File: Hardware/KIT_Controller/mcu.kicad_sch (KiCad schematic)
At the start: 27 parts, among them J201 USB_BOOT, J202 USB_B, U201 RP2040, U202 W25Q128JVS, U203 NCP1117-3.3_SOT223, Y201 Crystal

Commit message: add other junk idk
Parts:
- added U201: TCA9554DB, Package_SO:SSOP-16_5.3x6.2mm_P0.65mm, symbol Interface_Expansion:TCA9554DB
- added U204: HDSP-7401, Display_7Segment:HDSP-7401, symbol Display_Character:HDSP-7401
- renumbered C215 to C203, C214 to C204, C216 to C205, C203 to C206, C204 to C207, C205 to C208, C206 to C209, C207 to C210, C208 to C211, C209 to C212, C210 to C213, C211 to C214, C212 to C215, C213 to C216, J202 to J201, J201 to J202, R204 to R201, R205 to R202, R201 to R203, R202 to R204, R203 to R205, U201 to U205
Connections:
- no-connect marks 33 -> 59

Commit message: Add more stuff
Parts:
- added R206: 10k, Resistor_SMD:R_0805_2012Metric, symbol Device:R_Small
- added R207, R208, R209, R210, R211, R212, R213, R214: 240, Resistor_SMD:R_0805_2012Metric, symbol Device:R_Small
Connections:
- net +3V3: now also U201.16 (VDD), R206.2
- net GND: now also U201.1 (A0), U201.2 (A1), U201.3 (A2), U201.8 (GND), U204.1 (CA), U204.6 (CA)
- net at U201.10 (P5): now also R213.1
- net at U201.11 (P6): now also R210.1
- net at U201.12 (P7): now also R214.1
- net at U201.13 (~{INT}): now also R206.1
- net SCL: now reaches U201.14 (SCL)
- net SCL: now also U205.7 (GPIO5)
- net SDA: now reaches U201.15 (SDA)
- net SDA: now also U205.6 (GPIO4)
- net at U201.4 (P0): now also R207.1
- net at U201.5 (P1): now also R211.1
- net at U201.6 (P2): now also R208.1
- net at U201.7 (P3): now also R212.1
- net at U201.9 (P4): now also R209.1
- net MISO: now reaches U205.27 (GPIO16)
- net SCK: now reaches U205.29 (GPIO18)
- net MOSI: now reaches U205.30 (GPIO19)
- net at U204.10 (A): now also R207.2
- net at U204.2 (F): now also R213.2
- net at U204.3 (G): now also R210.2
- net at U204.4 (E): now also R209.2
- net at U204.5 (D): now also R212.2
- net at U204.7 (DP): now also R214.2
- net at U204.8 (C): now also R208.2
- net at U204.9 (B): now also R211.2
- no-connect marks 59 -> 28
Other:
- note added: "Clock"
- note added: "EEPROM"
- note added: "LLL corrosponds to Address 20 (32 in decimal)"
- note added: "USB"
- note added: "i2c status"
- company: (none) -> Kitsune Scientific
- title: (none) -> KIT Mainboard
- moved on the sheet: C206, C207, C208, C209, C210, C211, C212, C213, C214, C215, C216, R204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

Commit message: Fixup drc
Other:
- moved on the sheet: R207, R208, R209, R210
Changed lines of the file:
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@@
   (junction (at 172.085 36.83) (diameter 0) (color 0 0 0 0)
+  )
+  (junction (at 73.025 163.195) (diameter 0) (color 0 0 0 0)
   )
   (junction (at 24.13 178.435) (diameter 0) (color 0 0 0 0)
@@
     (stroke (width 0) (type default) (color 0 0 0 0))
   )
-  (wire (pts (xy 47.625 173.355) (xy 50.165 173.355))
+  (wire (pts (xy 47.625 173.355) (xy 52.07 173.355))
     (stroke (width 0) (type default) (color 0 0 0 0))
   )
@@
     (stroke (width 0) (type default) (color 0 0 0 0))
   )
-  (wire (pts (xy 55.245 163.195) (xy 73.025 163.195))
+  (wire (pts (xy 57.15 163.195) (xy 73.025 163.195))
     (stroke (width 0) (type default) (color 0 0 0 0))
   )
@@
     (stroke (width 0) (type default) (color 0 0 0 0))
   )
+  (wire (pts (xy 74.295 163.195) (xy 73.025 163.195))
+    (stroke (width 0) (type default) (color 0 0 0 0))
+  )
   (wire (pts (xy 36.83 78.74) (xy 46.99 78.74))
     (stroke (width 0) (type default) (color 0 0 0 0))
@@
     (stroke (width 0) (type default) (color 0 0 0 0))
   )
-  (wire (pts (xy 55.245 178.435) (xy 73.025 178.435))
+  (wire (pts (xy 57.15 178.435) (xy 73.025 178.435))
     (stroke (width 0) (type default) (color 0 0 0 0))
   )
@@
     (stroke (width 0) (type default) (color 0 0 0 0))
   )
-  (wire (pts (xy 47.625 178.435) (xy 50.165 178.435))
+  (wire (pts (xy 47.625 178.435) (xy 52.07 178.435))
     (stroke (width 0) (type default) (color 0 0 0 0))
   )
@@
     (stroke (width 0) (type default) (color 0 0 0 0))
   )
-  (wire (pts (xy 55.245 173.355) (xy 73.025 173.355))
+  (wire (pts (xy 57.15 173.355) (xy 73.025 173.355))
     (stroke (width 0) (type default) (color 0 0 0 0))
   )
@@
     (stroke (width 0) (type default) (color 0 0 0 0))
   )
-  (wire (pts (xy 55.245 168.275) (xy 73.025 168.275))
+  (wire (pts (xy 57.15 168.275) (xy 73.025 168.275))
     (stroke (width 0) (type default) (color 0 0 0 0))
   )
@@
     (stroke (width 0) (type default) (color 0 0 0 0))
   )
-  (wire (pts (xy 47.625 163.195) (xy 50.165 163.195))
+  (wire (pts (xy 47.625 163.195) (xy 52.07 163.195))
     (stroke (width 0) (type default) (color 0 0 0 0))
   )
@@
     (stroke (width 0) (type default) (color 0 0 0 0))
   )
-  (wire (pts (xy 47.625 168.275) (xy 50.165 168.275))
+  (wire (pts (xy 47.625 168.275) (xy 52.07 168.275))
     (stroke (width 0) (type default) (color 0 0 0 0))
   )
@@
     (pin "2")
   )
-  (symbol (lib_id "Device:R_Small") (at 52.705 173.355 90) (unit 1)
-    (in_bom yes) (on_board yes)
-    (property "Reference" "R209" (id 0) (at 49.53 172.085 90))
-    (property "Value" "240" (id 1) (at 52.705 173.355 90))
-    (property "Footprint" "Resistor_SMD:R_0805_2012Metric" (id 2) (at 52.705 173.355 0)
-      (effects (font (size 1.27 1.27)) hide)
-    )
-    (property "Datasheet" "~" (id 3) (at 52.705 173.355 0)
+  (symbol (lib_id "Device:R_Small") (at 54.61 173.355 90) (unit 1)
+    (in_bom yes) (on_board yes)
+    (property "Reference" "R209" (id 0) (at 50.165 172.085 90))
+    (property "Value" "240" (id 1) (at 54.61 173.355 90))
+    (property "Footprint" "Resistor_SMD:R_0805_2012Metric" (id 2) (at 54.61 173.355 0)
+      (effects (font (size 1.27 1.27)) hide)
+    )
+    (property "Datasheet" "~" (id 3) (at 54.61 173.355 0)
       (effects (font (size 1.27 1.27)) hide)
     )
@@
   (symbol (lib_id "Device:R_Small") (at 64.135 175.895 90) (unit 1)
     (in_bom yes) (on_board yes)
-    (property "Reference" "R213" (id 0) (at 60.96 174.625 90))
+    (property "Reference" "R213" (id 0) (at 59.69 174.625 90))
     (property "Value" "240" (id 1) (at 64.135 175.895 90))
     (property "Footprint" "Resistor_SMD:R_0805_2012Metric" (id 2) (at 64.135 175.895 0)
@@
     (pin "2")
   )
-  (symbol (lib_id "Device:R_Small") (at 52.705 163.195 90) (unit 1)
-    (in_bom yes) (on_board yes)
-    (property "Reference" "R207" (id 0) (at 49.53 161.925 90))
-    (property "Value" "240" (id 1) (at 52.705 163.195 90))
-    (property "Footprint" "Resistor_SMD:R_0805_2012Metric" (id 2) (at 52.705 163.195 0)
-      (effects (font (size 1.27 1.27)) hide)
-    )
-    (property "Datasheet" "~" (id 3) (at 52.705 163.195 0)
+  (symbol (lib_id "Device:R_Small") (at 54.61 163.195 90) (unit 1)
+    (in_bom yes) (on_board yes)
+    (property "Reference" "R207" (id 0) (at 50.165 161.925 90))
+    (property "Value" "240" (id 1) (at 54.61 163.195 90))
+    (property "Footprint" "Resistor_SMD:R_0805_2012Metric" (id 2) (at 54.61 163.195 0)
+      (effects (font (size 1.27 1.27)) hide)
+    )
+    (property "Datasheet" "~" (id 3) (at 54.61 163.195 0)
       (effects (font (size 1.27 1.27)) hide)
     )
@@
   (symbol (lib_id "Device:R_Small") (at 64.135 165.735 90) (unit 1)
     (in_bom yes) (on_board yes)
-    (property "Reference" "R211" (id 0) (at 60.96 164.465 90))
+    (property "Reference" "R211" (id 0) (at 59.69 164.465 90))
     (property "Value" "240" (id 1) (at 64.135 165.735 90))
     (property "Footprint" "Resistor_SMD:R_0805_2012Metric" (id 2) (at 64.135 165.735 0)
@@
     (pin "3")
   )
-  (symbol (lib_id "Device:R_Small") (at 52.705 178.435 90) (unit 1)
-    (in_bom yes) (on_board yes)
-    (property "Reference" "R210" (id 0) (at 49.53 177.165 90))
-    (property "Value" "240" (id 1) (at 52.705 178.435 90))
-    (property "Footprint" "Resistor_SMD:R_0805_2012Metric" (id 2) (at 52.705 178.435 0)
-      (effects (font (size 1.27 1.27)) hide)
-    )
-    (property "Datasheet" "~" (id 3) (at 52.705 178.435 0)
+  (symbol (lib_id "Device:R_Small") (at 54.61 178.435 90) (unit 1)
+    (in_bom yes) (on_board yes)
+    (property "Reference" "R210" (id 0) (at 50.165 177.165 90))
+    (property "Value" "240" (id 1) (at 54.61 178.435 90))
+    (property "Footprint" "Resistor_SMD:R_0805_2012Metric" (id 2) (at 54.61 178.435 0)
+      (effects (font (size 1.27 1.27)) hide)
+    )
+    (property "Datasheet" "~" (id 3) (at 54.61 178.435 0)
       (effects (font (size 1.27 1.27)) hide)
     )
@@
   (symbol (lib_id "Device:R_Small") (at 64.135 170.815 90) (unit 1)
     (in_bom yes) (on_board yes)
-    (property "Reference" "R212" (id 0) (at 60.96 169.545 90))
+    (property "Reference" "R212" (id 0) (at 59.69 169.545 90))
     (property "Value" "240" (id 1) (at 64.135 170.815 90))
     (property "Footprint" "Resistor_SMD:R_0805_2012Metric" (id 2) (at 64.135 170.815 0)
@@
   (symbol (lib_id "Device:R_Small") (at 64.135 180.975 90) (unit 1)
     (in_bom yes) (on_board yes)
-    (property "Reference" "R214" (id 0) (at 60.96 179.705 90))
+    (property "Reference" "R214" (id 0) (at 59.69 179.705 90))
     (property "Value" "240" (id 1) (at 64.135 180.975 90))
     (property "Footprint" "Resistor_SMD:R_0805_2012Metric" (id 2) (at 64.135 180.975 0)
@@
     (pin "1")
   )
-  (symbol (lib_id "Device:R_Small") (at 52.705 168.275 90) (unit 1)
-    (in_bom yes) (on_board yes)
-    (property "Reference" "R208" (id 0) (at 49.53 167.005 90))
-    (property "Value" "240" (id 1) (at 52.705 168.275 90))
-    (property "Footprint" "Resistor_SMD:R_0805_2012Metric" (id 2) (at 52.705 168.275 0)
-      (effects (font (size 1.27 1.27)) hide)
-    )
-    (property "Datasheet" "~" (id 3) (at 52.705 168.275 0)
-      (effects (font (size 1.27 1.27)) hide)
-    )
+  (symbol (lib_id "Device:R_Small") (at 54.61 168.275 90) (unit 1)
+    (in_bom yes) (on_board yes)
+    (property "Reference" "R208" (id 0) (at 50.165 167.005 90))
+    (property "Value" "240" (id 1) (at 54.61 168.275 90))
+    (property "Footprint" "Resistor_SMD:R_0805_2012Metric" (id 2) (at 54.61 168.275 0)
+      (effects (font (size 1.27 1.27)) hide)
+    )
+    (property "Datasheet" "~" (id 3) (at 54.61 168.275 0)
+      (effects (font (size 1.27 1.27)) hide)
+    )

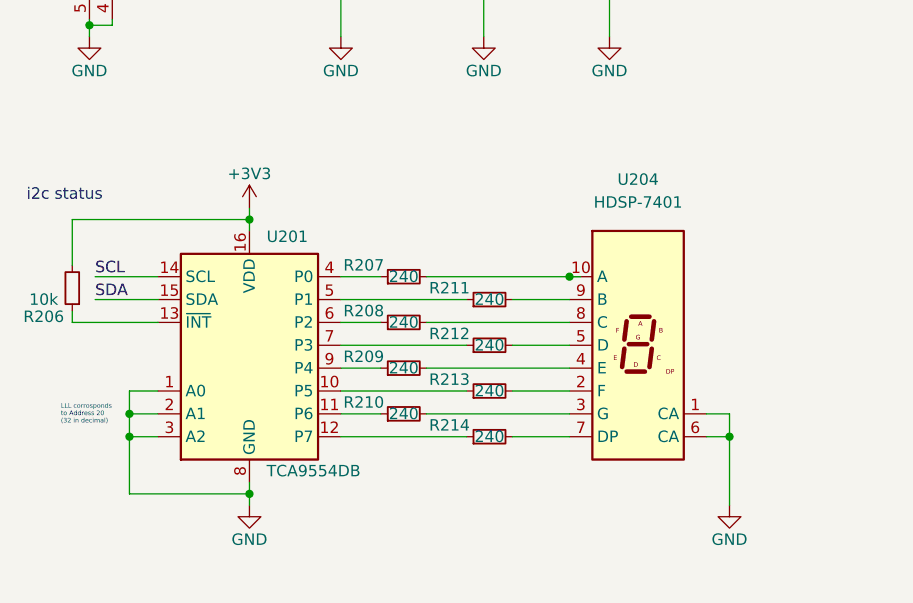
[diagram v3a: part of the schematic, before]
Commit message: Add short range modem
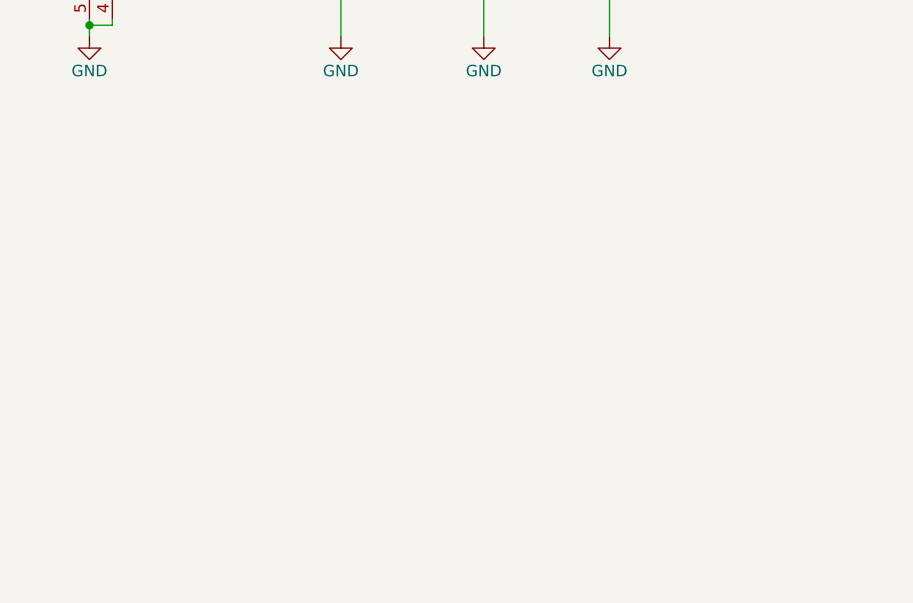
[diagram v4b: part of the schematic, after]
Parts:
- removed R206: 10k, Resistor_SMD:R_0805_2012Metric, symbol Device:R_Small
- removed R207, R208, R209, R210, R211, R212, R213, R214: 240, Resistor_SMD:R_0805_2012Metric, symbol Device:R_Small
- removed U201: TCA9554DB, Package_SO:SSOP-16_5.3x6.2mm_P0.65mm, symbol Interface_Expansion:TCA9554DB
- removed U204: HDSP-7401, Display_7Segment:HDSP-7401, symbol Display_Character:HDSP-7401
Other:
- note removed: "LLL corrosponds to Address 20 (32 in decimal)"
- note removed: "i2c status"
